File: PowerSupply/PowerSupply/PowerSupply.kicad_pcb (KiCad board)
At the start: 2 copper layers, 61.1 x 61.3 mm, 47 parts, among them J1 Conn_01x04_Female, J2 ATX24, J3 PS_ON, P1 MAX9939, Q1 SI7157DP, Q2 SIRA32DP, Q3 SIRA32DP, Q4 SIRA32DP, Q5 MMBT3904, Q6 MMBT3904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

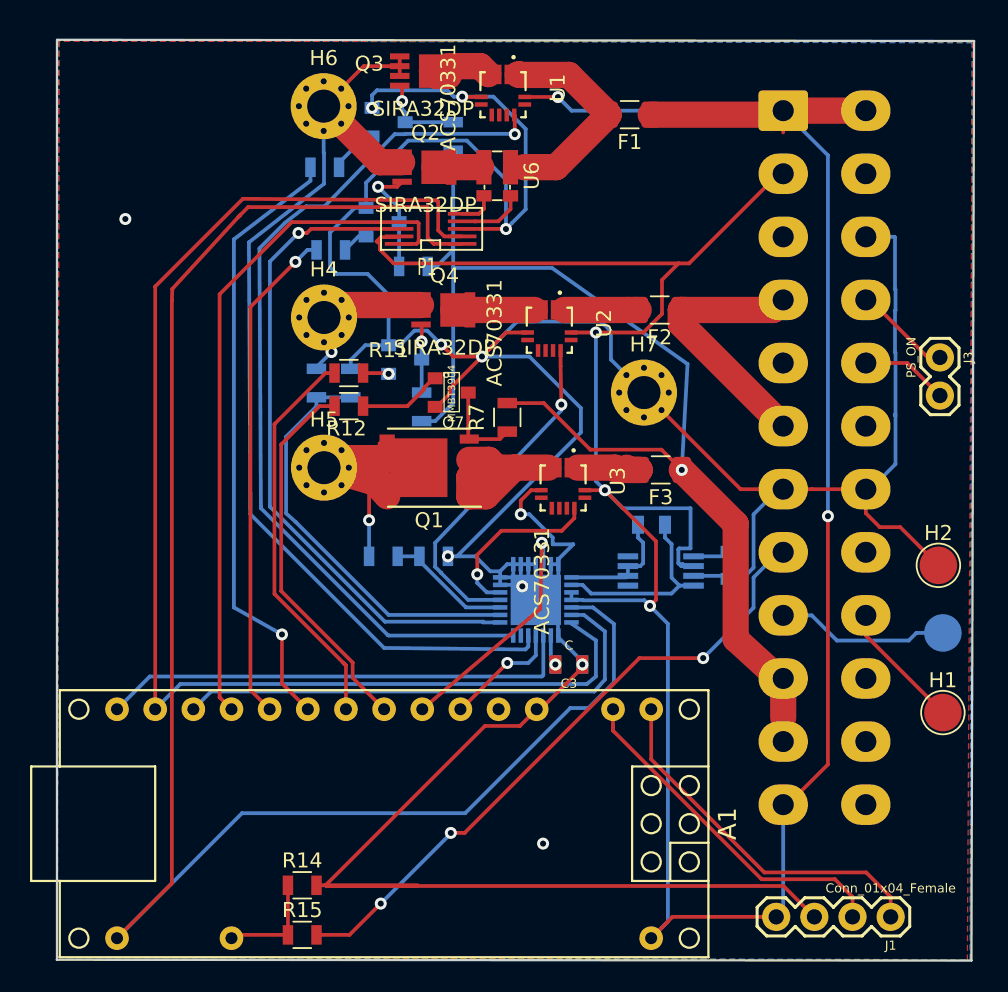
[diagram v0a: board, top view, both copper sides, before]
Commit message: Updated Door Unlocker and PS
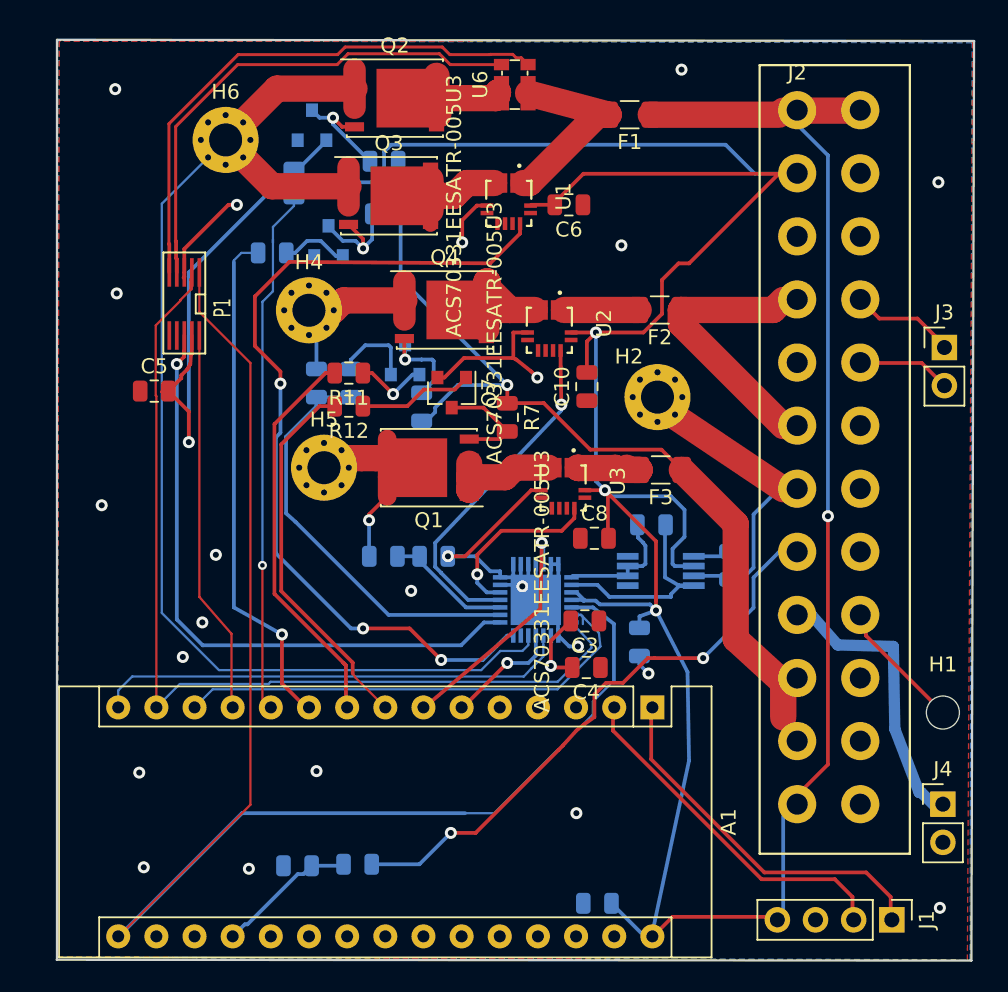
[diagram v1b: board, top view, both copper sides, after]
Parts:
- removed H3: 5V_USB, TestPoint:TestPoint_Pad_D2.5mm
- removed H7: GND_OUT, MountingHole:MountingHole_2.2mm_M2_Pad_Via
- added C10: C, Capacitor_SMD:C_0805_2012Metric, F.Cu at (222.5, 109.6)
- added C5: C, Capacitor_SMD:C_0805_2012Metric, F.Cu at (193.7, 109.9)
- added C6: C, Capacitor_SMD:C_0805_2012Metric, F.Cu at (221.3, 97.5)
- added C7: C, Capacitor_SMD:C_0805_2012Metric, B.Cu at (223.2, 144.0)
- added C8: C, Capacitor_SMD:C_0805_2012Metric, F.Cu at (223.0, 119.7)
- added C9: C, Capacitor_SMD:C_0805_2012Metric, B.Cu at (226.0, 126.6)
- added J4: Conn_01x02_Female, Connector_PinHeader_2.54mm:PinHeader_1x02_P2.54mm_Vertical, F.Cu at (246.2, 137.4)
- A1: footprint CustomPS:arduino_nano -> Module:Arduino_Nano
- C1, C2, C3: footprint Capacitors:0805 -> Capacitor_SMD:C_0805_2012Metric
- C4: footprint Capacitors:0805 -> Capacitor_SMD:C_0805_2012Metric; moved to F.Cu
- F1, F2, F3: footprint Fuse:Fuse_1206_3216Metric -> Resistor_SMD:R_1206_3216Metric
- H1: value 5V_load -> MountingHole_Pad; footprint TestPoint:TestPoint_Pad_D2.5mm -> MountingHole:MountingHole_2.2mm_M2
- H2: value 5V_load_GND -> MountingHole_Pad; footprint TestPoint:TestPoint_Pad_D2.5mm -> MountingHole:MountingHole_2.2mm_M2_Pad_Via
- H4: value 5V_OUT -> MountingHole_Pad
- H5: value 12V_OUT -> MountingHole_Pad
- H6: value 3p3V_OUT -> MountingHole_Pad
- J1: footprint Connectors2:1X04 -> Connector_PinHeader_2.54mm:PinHeader_1x04_P2.54mm_Vertical
- J2: footprint Connector_Molex:Molex_Mini-Fit_Jr_5566-24A_2x12_P4.20mm_Vertical -> CustomPS:ATX_24Pin; moved to F.Cu
- J3: value PS_ON -> Conn_01x02_Female; footprint Connectors2:1X02 -> Connector_PinHeader_2.54mm:PinHeader_1x02_P2.54mm_Vertical
- Q1: footprint SMD_Packages:SO-8_PowerPAK_Vishay_Single -> CustomPS:Vishay_PowerPAK_SO-8
- Q2, Q3, Q4: footprint kicad-open-modules:PowerPAK-1212-8 -> CustomPS:Vishay_PowerPAK_SO-8
- Q5, Q6, Q7, Q8: value MMBT3904 -> BC817; footprint SMD_Packages_oj:SOT23 -> Package_TO_SOT_SMD:SOT-23
- R1, R2, R3, R4, R5, R6, R7, R9: value 10k -> R; footprint Resistors_SMD:R_0805 -> Resistor_SMD:R_0805_2012Metric
- R10, R11, R12, R13: value 2.2k -> R; footprint Resistors_SMD:R_0805 -> Resistor_SMD:R_0805_2012Metric
- R14, R15: footprint Resistors_SMD:R_0805 -> Resistor_SMD:R_0805_2012Metric; moved to B.Cu
- U1, U2, U3: value ACS70331 -> ACS70331EESATR-005U3
- U5: footprint CustomFP:MAX6126B30&plus_ -> Package_SO:MSOP-8_3x3mm_P0.65mm
- moved H2 21.8 mm to (227.2, 110.3)
- moved A1 19.5 mm to (226.9, 131.0), turned to 270 degrees
- moved P1 17.1 mm to (195.7, 104.1), turned to 180 degrees
- moved Q5 8.85 mm to (205.3, 99.9)
- moved Q3 8.61 mm to (209.3, 96.9)
- moved Q8 7.98 mm to (204.2, 92.2)
- moved R9 7.27 mm to (209.0, 94.6)
- moved U1 7.24 mm to (217.3, 97.4)
- moved H6 6.90 mm to (198.5, 93.2)
- moved R5 6.81 mm to (209.2, 98.1), turned to 180 degrees
- moved R10 6.69 mm to (201.6, 100.7)
- moved U6 6.18 mm to (217.7, 89.5), turned to 90 degrees
- moved R15 5.97 mm to (207.2, 141.4)
- moved R13 5.08 mm to (203.0, 96.0), turned to 270 degrees
- moved Q2 5.04 mm to (209.7, 90.4)
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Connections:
- net Net-(P1-Pad4) renamed /Sense3V3-
- net Net-(P1-Pad5) renamed /Sense3V3+
- Q1 pad 1: /12VA_S -> Net-(Q1-Pad1)
- Q1 pad 3: /12VA_S -> 12V_Out
- Q7 pad 3: Net-(Q1-Pad4) -> Net-(Q1-Pad1)
- R7 pad 2: Net-(Q1-Pad4) -> Net-(Q1-Pad1)
- U6 pad 1: /3.3V_A -> /3.3VA_D1
- U6 pad 4: /3.3VA_D1 -> /3.3V_A
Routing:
- net GND: track 271.8 -> 87.2 mm, vias 11 -> 23
- net +3V3: track 203.7 -> 257.6 mm
- net /Sense3V3+: track 2.44 -> 36.4 mm
- net /Sense3V3-: track 4.02 -> 33.7 mm
- net SPI_MOSI_PINX: track 87.8 -> 63.9 mm
- net +12V: track 81.0 -> 60.6 mm
- net SPI_3V3_CS_PINX: track 45.8 -> 25.7 mm
- net SPI_Clk_PINX: track 116.0 -> 97.1 mm
- net 3V3_Out: track 66.9 -> 85.1 mm
- net 12V_Out: track 26.0 -> 16.0 mm
- net 5V_USB: track 11.5 -> 19.7 mm
- net Net-(Q1-Pad1): track 0.00 -> 7.80 mm
- net 3V3_COURSE_EN: track 41.2 -> 34.3 mm
- net Net-(Q1-Pad4): track 6.04 -> 0.00 mm
- net /3.3VA_D1: track 4.42 -> 10.2 mm
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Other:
- net class Signal added: clearance 0.2, trace_width 0.152, via_dia 0.6, via_drill 0.3
- rule trace_min: 0.2 -> 0
- rule via_min_drill: 0.3 -> 0.2
- rule via_min_size: 0.4 -> 0.45
